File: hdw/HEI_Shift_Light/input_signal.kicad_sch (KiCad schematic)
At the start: 20 parts

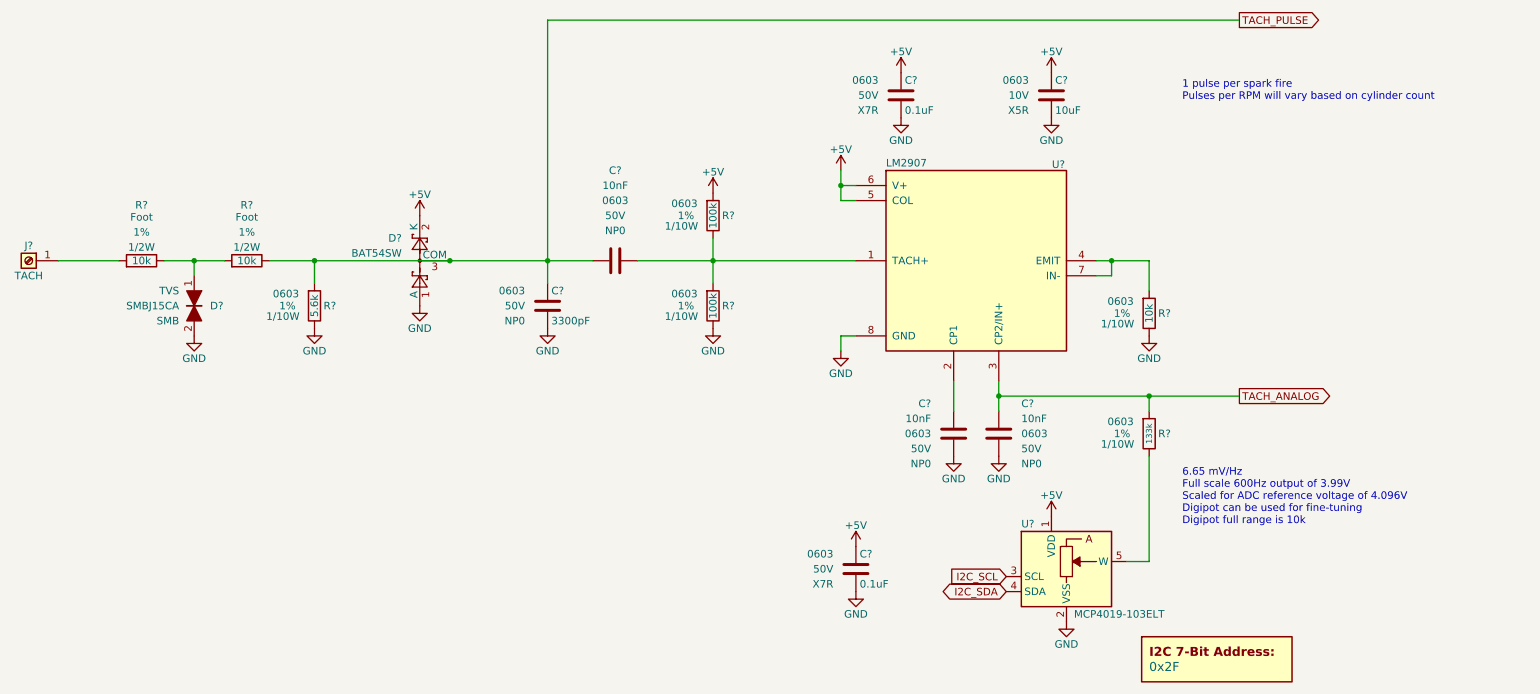
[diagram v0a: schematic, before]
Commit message: filled in digikey part numbers
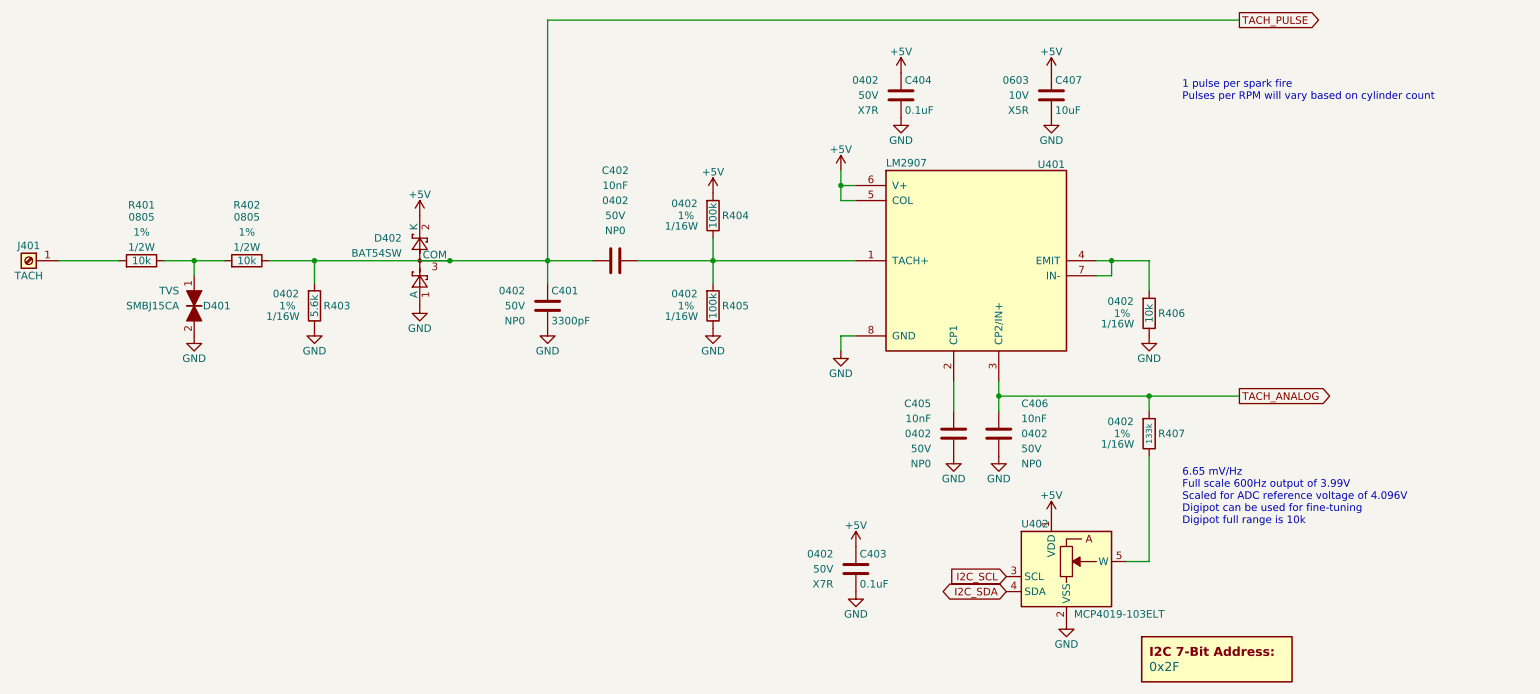
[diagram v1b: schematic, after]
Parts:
- C401: renamed from C?; footprint (none) -> Capacitors_SMD:C_0402; Digi-Key PN PN -> 311-3968-1-ND; display_footprint 0603 -> 0402
- C402, C405, C406: renamed from C?; footprint (none) -> Capacitors_SMD:C_0402; display_footprint 0603 -> 0402
- C403, C404: renamed from C?; footprint Capacitors_SMD:C_0603 -> Capacitors_SMD:C_0402; display_footprint 0603 -> 0402
- D401: renamed from D?; Digi-Key PN (none) -> SMBJ15CA-E3-52GICT-ND; Footprint Display SMB -> (none); display_footprint (none) -> SMB
- D402: renamed from D?; Digi-Key PN (none) -> 568-1615-1-ND
- J401: renamed from J?; footprint (none) -> Keystone:7691; Digi-Key PN (none) -> 36-7691-ND; MPN (none) -> 7691; Manufacturer (none) -> Keystone Electronics
- R401, R402: renamed from R?; footprint (none) -> Resistors_SMD:R_0805; Digi-Key PN (none) -> 541-10.0KLCT-ND; display_footprint Foot -> 0805
- R403: renamed from R?; footprint Resistors_SMD:R_0603 -> Resistors_SMD:R_0402; Digi-Key PN (none) -> 541-5.60KLCT-ND; Wattage 1/10W -> 1/16W; display_footprint 0603 -> 0402
- R404, R405: renamed from R?; footprint Resistors_SMD:R_0603 -> Resistors_SMD:R_0402; Digi-Key PN (none) -> 541-100KLCT-ND; Wattage 1/10W -> 1/16W; display_footprint 0603 -> 0402
- R406: renamed from R?; footprint Resistors_SMD:R_0603 -> Resistors_SMD:R_0402; Digi-Key PN 541-10.0KHCT-ND -> 541-10.0KLCT-ND; Wattage 1/10W -> 1/16W; display_footprint 0603 -> 0402
- R407: renamed from R?; footprint Resistors_SMD:R_0603 -> Resistors_SMD:R_0402; Digi-Key PN (none) -> 541-133KLCT-ND; Wattage 1/10W -> 1/16W; display_footprint 0603 -> 0402
- U401: renamed from U?; Digi-Key PN (none) -> LM2907N-8-NOPB-ND
- gave numbers to parts that had none: 3

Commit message: fixed a few digikey pns
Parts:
- R401, R402: Digi-Key PN 541-10.0KLCT-ND -> P16059CT-ND; MPN (none) -> CRCW080510K0FKEA
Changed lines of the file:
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@@
 			)
 		)
-		(property "Digi-Key PN" "541-10.0KLCT-ND"
+		(property "Digi-Key PN" "P16059CT-ND"
 			(at 30.48 101.6 0)
 			(hide yes)
@@
 			)
 		)
+    (property "MPN" "CRCW080510K0FKEA" (at 40.64 93.98 0)
+      (effects (font (size 1.27 1.27)) (hide yes))
+    )
 		(pin "1"
 		)
@@
 			)
 		)
-		(property "Digi-Key PN" "541-10.0KLCT-ND"
+		(property "Digi-Key PN" "P16059CT-ND"
 			(at 48.26 101.6 0)
 			(hide yes)
@@
 			)
 		)
-		(pin "1"
-		)
+    (property "MPN" "CRCW080510K0FKEA" (at 58.42 93.98 0)
+      (effects (font (size 1.27 1.27)) (hide yes))
+    )
+		(pin "1"
+		)

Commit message: Added input signal path simulation
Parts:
- C406: value 10nF -> 1uF; Digi-Key PN 311-3960-1-ND -> (none); display_footprint 0402 -> (none)
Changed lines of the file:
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@@
 			)
 		)
-    (property "Digi-Key PN" "SMBJ15CA-E3-52GICT-ND" (at 49.53 101.6 0)
-      (effects (font (size 1.27 1.27)) (hide yes))
-    )
+		(property "Digi-Key PN" "SMBJ15CA-E3-52GICT-ND"
+			(at 49.53 101.6 0)
+			(hide yes)
+			(show_name no)
+			(do_not_autoplace no)
+			(effects
+				(font
+					(size 1.27 1.27)
+				)
+			)
+		)
 		(pin "1"
 		)
@@
 			)
 		)
-    (property "MPN" "CRCW080510K0FKEA" (at 40.64 93.98 0)
-      (effects (font (size 1.27 1.27)) (hide yes))
-    )
+		(property "MPN" "CRCW080510K0FKEA"
+			(at 40.64 93.98 0)
+			(hide yes)
+			(show_name no)
+			(do_not_autoplace no)
+			(effects
+				(font
+					(size 1.27 1.27)
+				)
+			)
+		)
 		(pin "1"
 		)
@@
 			)
 		)
-    (property "Digi-Key PN" "568-1615-1-ND" (at 87.63 93.98 0)
-      (effects (font (size 1.27 1.27)) (hide yes))
-    )
+		(property "Digi-Key PN" "568-1615-1-ND"
+			(at 87.63 93.98 0)
+			(hide yes)
+			(show_name no)
+			(do_not_autoplace no)
+			(effects
+				(font
+					(size 1.27 1.27)
+				)
+			)
+		)
 		(pin "1"
 		)
@@
 			)
 		)
-    (property "Digi-Key PN" "LM2907N-8-NOPB-ND" (at 181.61 93.98 0)
-      (effects (font (size 1.27 1.27)) (hide yes))
-    )
+		(property "Digi-Key PN" "LM2907N-8-NOPB-ND"
+			(at 181.61 93.98 0)
+			(hide yes)
+			(show_name no)
+			(do_not_autoplace no)
+			(effects
+				(font
+					(size 1.27 1.27)
+				)
+			)
+		)
 		(pin "7"
 		)
@@
 			)
 		)
-		(property "Value" "10nF"
+		(property "Value" "1uF"
 			(at 189.23 120.6499 0)
 			(show_name no)
@@
 			)
 		)
-		(property "display_footprint" "0402"
+		(property "display_footprint" ""
 			(at 189.23 123.1899 0)
 			(show_name no)
@@
 			)
 		)
-		(property "Digi-Key PN" "311-3960-1-ND"
+		(property "Digi-Key PN" ""
 			(at 196.215 110.49 0)
 			(hide yes)
@@
 			)
 		)
-    (property "Digi-Key PN" "36-7691-ND" (at 21.59 93.98 0)
-      (effects (font (size 1.27 1.27)) (hide yes))
-    )
-    (property "MPN" "7691" (at 21.59 93.98 0)
-      (effects (font (size 1.27 1.27)) (hide yes))
-    )
-    (property "Manufacturer" "Keystone Electronics" (at 21.59 93.98 0)
-      (effects (font (size 1.27 1.27)) (hide yes))
-    )
+		(property "Digi-Key PN" "36-7691-ND"
+			(at 21.59 93.98 0)
+			(hide yes)
+			(show_name no)
+			(do_not_autoplace no)
+			(effects
+				(font
+					(size 1.27 1.27)
+				)
+			)
+		)
+		(property "MPN" "7691"
+			(at 21.59 93.98 0)
+			(hide yes)
+			(show_name no)
+			(do_not_autoplace no)
+			(effects
+				(font
+					(size 1.27 1.27)
+				)
+			)
+		)
+		(property "Manufacturer" "Keystone Electronics"
+			(at 21.59 93.98 0)
+			(hide yes)
+			(show_name no)
+			(do_not_autoplace no)
+			(effects
+				(font
+					(size 1.27 1.27)
+				)
+			)
+		)
 		(pin "1"
 		)
@@
 			)
 		)
-    (property "MPN" "CRCW080510K0FKEA" (at 58.42 93.98 0)
-      (effects (font (size 1.27 1.27)) (hide yes))
-    )
+		(property "MPN" "CRCW080510K0FKEA"
+			(at 58.42 93.98 0)
+			(hide yes)
+			(show_name no)
+			(do_not_autoplace no)
+			(effects
+				(font
+					(size 1.27 1.27)
+				)
+			)
+		)
 		(pin "1"
 		)

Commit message: change LM2907 filter cap to 10uF
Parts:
- removed C406: 1uF, Capacitors_SMD:C_0402, symbol Custom Library:C_Custom
- added C406: 10uF, Capacitors_SMD:C_0603, symbol Custom_Library:C_Custom
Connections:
- net GND: now also C406.2
- net TACH_ANALOG: now also C406.1
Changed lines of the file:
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@@
-	)
-	(symbol
-		(lib_id "Custom Library:C_Custom")
-		(at 185.42 123.19 0)
-		(unit 1)
-		(body_style 1)
-		(exclude_from_sim no)
-		(in_bom yes)
-		(on_board yes)
-		(in_pos_files yes)
-		(dnp no)
-		(property "Reference" "C406"
-			(at 189.23 118.1099 0)
-			(show_name no)
-			(do_not_autoplace no)
-			(effects
-				(font
-					(size 1.27 1.27)
-				)
-				(justify left)
-			)
-		)
-		(property "Value" "1uF"
-			(at 189.23 120.6499 0)
-			(show_name no)
-			(do_not_autoplace no)
-			(effects
-				(font
-					(size 1.27 1.27)
-				)
-				(justify left)
-			)
-		)
-		(property "Footprint" "Capacitors_SMD:C_0402"
-			(at 186.3852 127 0)
-			(hide yes)
-			(show_name no)
-			(do_not_autoplace no)
-			(effects
-				(font
-					(size 1.27 1.27)
-				)
-			)
-		)
-		(property "Datasheet" ""
-			(at 186.055 120.65 0)
-			(hide yes)
-			(show_name no)
-			(do_not_autoplace no)
-			(effects
-				(font
-					(size 1.27 1.27)
-				)
-			)
-		)
-		(property "Description" "Unpolarized capacitor"
-			(at 185.42 123.19 0)
-			(hide yes)
-			(show_name no)
-			(do_not_autoplace no)
-			(effects
-				(font
-					(size 1.27 1.27)
-				)
-			)
-		)
-		(property "display_footprint" ""
-			(at 189.23 123.1899 0)
-			(show_name no)
-			(do_not_autoplace no)
-			(effects
-				(font
-					(size 1.27 1.27)
-				)
-				(justify left)
-			)
-		)
-		(property "Voltage" "50V"
-			(at 189.23 125.7299 0)
-			(show_name no)
-			(do_not_autoplace no)
-			(effects
-				(font
-					(size 1.27 1.27)
-				)
-				(justify left)
-			)
-		)
-		(property "Dielectric" "NP0"
-			(at 189.23 128.2699 0)
-			(show_name no)
-			(do_not_autoplace no)
-			(effects
-				(font
-					(size 1.27 1.27)
-				)
-				(justify left)
-			)
-		)
-		(property "Digi-Key PN" ""
-			(at 196.215 110.49 0)
-			(hide yes)
-			(show_name no)
-			(do_not_autoplace no)
-			(effects
-				(font
-					(size 1.524 1.524)
-				)
-			)
-		)
-		(pin "1"
-		)
-		(pin "2"
-		)
-		(instances
-			(project "HEI_Shift_Light"
-				(path "/288c8230-69eb-4ad9-929d-f4630114196f/3f3e3aac-043b-4713-af21-26e9e85000ef"
-					(reference "C406")
-					(unit 1)
-				)
-			)
-		)
 	)
 	(symbol
@@
 					(unit 1)
 				)
+			)
+		)
+	)
+	(symbol
+		(lib_id "Custom_Library:C_Custom")
+		(at 185.42 123.19 0)
+		(unit 1)
+		(body_style 1)
+		(exclude_from_sim no)
+		(in_bom yes)
+		(on_board yes)
+		(in_pos_files yes)
+		(dnp no)
+		(fields_autoplaced yes)
+		(property "Reference" "C406"
+			(at 189.23 118.1099 0)
+			(show_name no)
+			(do_not_autoplace no)
+			(effects
+				(font
+					(size 1.27 1.27)
+				)
+				(justify left)
+			)
+		)
+		(property "Value" "10uF"
+			(at 189.23 120.6499 0)
+			(show_name no)
+			(do_not_autoplace no)
+			(effects
+				(font
+					(size 1.27 1.27)
+				)
+				(justify left)
+			)
+		)
+		(property "Footprint" "Capacitors_SMD:C_0603"
+			(at 186.3852 127 0)
+			(hide yes)
+			(show_name no)
+			(do_not_autoplace no)
+			(effects
+				(font
+					(size 1.27 1.27)
+				)
+			)
+		)
+		(property "Datasheet" ""
+			(at 186.055 120.65 0)
+			(hide yes)
+			(show_name no)
+			(do_not_autoplace no)
+			(effects
+				(font
+					(size 1.27 1.27)
+				)
+			)
+		)
+		(property "Description" ""
+			(at 185.42 123.19 0)
+			(show_name no)
+			(do_not_autoplace no)
+			(effects
+				(font
+					(size 1.27 1.27)
+				)
+			)
+		)
+		(property "display_footprint" "0603"
+			(at 189.23 123.1899 0)
+			(show_name no)
+			(do_not_autoplace no)
+			(effects
+				(font
+					(size 1.27 1.27)
+				)
+				(justify left)
+			)
+		)
+		(property "Voltage" "10V"
+			(at 189.23 125.7299 0)
+			(show_name no)
+			(do_not_autoplace no)
+			(effects
+				(font
+					(size 1.27 1.27)
+				)
+				(justify left)
+			)
+		)
+		(property "Dielectric" "X5R"
+			(at 189.23 128.2699 0)
+			(show_name no)
+			(do_not_autoplace no)
+			(effects
+				(font
+					(size 1.27 1.27)
+				)
+				(justify left)
+			)
+		)
+		(property "Digi-Key PN" "490-10474-1-ND"
+			(at 185.42 123.19 0)
+			(hide yes)
+			(show_name no)
+			(do_not_autoplace no)
+			(effects
+				(font
+					(size 1.27 1.27)
+				)
+			)
+		)
+		(pin "1"
+		)
+		(pin "2"
+		)
+		(instances
+			(project "HEI_Shift_Light"
+				(path "/288c8230-69eb-4ad9-929d-f4630114196f/3f3e3aac-043b-4713-af21-26e9e85000ef"
+					(reference "C406")
+					(unit 1)
+				)

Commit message: fixed some digikey pns
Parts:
- C401: Digi-Key PN 311-3968-1-ND -> 490-GRM1555C1H332GE01DTR-ND
- C403, C404: Digi-Key PN 399-7845-1-ND -> 1276-7069-1-ND
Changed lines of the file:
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@@
 			)
 		)
-		(property "Digi-Key PN" "399-7845-1-ND"
+		(property "Digi-Key PN" "1276-7069-1-ND"
 			(at 179.705 53.34 0)
 			(hide yes)
@@
 			)
 		)
-		(property "Digi-Key PN" "311-3968-1-ND"
+		(property "Digi-Key PN" "490-GRM1555C1H332GE01DTR-ND"
 			(at 120.015 88.9 0)
 			(hide yes)
@@
 			)
 		)
-		(property "Digi-Key PN" "399-7845-1-ND"
+		(property "Digi-Key PN" "1276-7069-1-ND"
 			(at 172.085 133.35 0)
 			(hide yes)

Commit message: added component datasheet properties
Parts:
- C403, C404: Digi-Key PN 1276-7069-1-ND -> 445-5932-1-ND
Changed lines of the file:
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@@
 			)
 		)
-		(property "Datasheet" ""
+		(property "Datasheet" "https://www.vishay.com/docs/88392/smbj.pdf"
 			(at 53.34 101.6 0)
 			(show_name no)
@@
 			)
 		)
-		(property "Datasheet" ""
+		(property "Datasheet" "https://product.tdk.com/en/system/files/dam/doc/product/capacitor/ceramic/mlcc/charasheet/c1005x7r1h104k050bb.pdf"
 			(at 169.545 63.5 0)
 			(hide yes)
@@
 			)
 		)
-		(property "Digi-Key PN" "1276-7069-1-ND"
+		(property "Digi-Key PN" "445-5932-1-ND"
 			(at 179.705 53.34 0)
 			(hide yes)
@@
 			)
 		)
-		(property "Datasheet" ""
+		(property "Datasheet" "https://www.vishay.com/docs/20035/dcrcwe3.pdf"
 			(at 210.82 123.19 0)
 			(hide yes)
@@
 			)
 		)
-		(property "Datasheet" ""
+		(property "Datasheet" "https://industrial.panasonic.com/cdbs/www-data/pdf/AQA0000/AQA0000CE21.pdf"
 			(at 40.64 93.98 0)
 			(hide yes)
@@
 			)
 		)
-		(property "Datasheet" ""
+		(property "Datasheet" "https://www.vishay.com/docs/20035/dcrcwe3.pdf"
 			(at 137.16 101.6 0)
 			(hide yes)
@@
 			)
 		)
-		(property "Datasheet" ""
+		(property "Datasheet" "https://www.vishay.com/docs/20035/dcrcwe3.pdf"
 			(at 137.16 86.36 0)
 			(hide yes)
@@
 			)
 		)
-		(property "Datasheet" ""
+		(property "Datasheet" "https://search.murata.co.jp/Ceramy/image/img/A01X/G101/ENG/GRM1555C1H332GE01-01A.pdf"
 			(at 109.855 99.06 0)
 			(hide yes)
@@
 			)
 		)
-		(property "Datasheet" ""
+		(property "Datasheet" "https://product.tdk.com/en/system/files/dam/doc/product/capacitor/ceramic/mlcc/charasheet/c1005x7r1h104k050bb.pdf"
 			(at 161.925 143.51 0)
 			(hide yes)
@@
 			)
 		)
-		(property "Digi-Key PN" "1276-7069-1-ND"
+		(property "Digi-Key PN" "445-5932-1-ND"
 			(at 172.085 133.35 0)
 			(hide yes)
@@
 			)
 		)
-		(property "Datasheet" ""
+		(property "Datasheet" "https://search.murata.co.jp/Ceramy/image/img/A01X/G101/ENG/GRM188R61A106KE69-01.pdf"
 			(at 194.945 63.5 0)
 			(hide yes)
@@
 			)
 		)
-		(property "Datasheet" ""
+		(property "Datasheet" "https://search.murata.co.jp/Ceramy/image/img/A01X/G101/ENG/GRM188R61A106KE69-01.pdf"
 			(at 186.055 120.65 0)
 			(hide yes)
@@
 			)
 		)
-		(property "Datasheet" ""
+		(property "Datasheet" "https://www.yageo.com/en/Chart/Download/pdf/CC0603JRNPO9BN103"
 			(at 118.11 94.615 0)
 			(hide yes)
@@
 			)
 		)
-		(property "Datasheet" ""
+		(property "Datasheet" "https://www.vishay.com/docs/20035/dcrcwe3.pdf"
 			(at 69.85 101.6 0)
 			(hide yes)
@@
 			)
 		)
-		(property "Datasheet" ""
+		(property "Datasheet" "https://www.vishay.com/docs/20035/dcrcwe3.pdf"
 			(at 210.82 102.87 0)
 			(hide yes)
@@
 			)
 		)
-		(property "Datasheet" ""
+		(property "Datasheet" "https://www.yageo.com/en/Chart/Download/pdf/CC0603JRNPO9BN103"
 			(at 177.165 120.65 0)
 			(hide yes)
@@
 			)
 		)
-		(property "Datasheet" ""
+		(property "Datasheet" "https://www.keyelco.com/userAssets/file/K75p73.pdf"
 			(at 21.59 93.98 0)
 			(hide yes)
@@
 			)
 		)
-		(property "Datasheet" ""
+		(property "Datasheet" "https://industrial.panasonic.com/cdbs/www-data/pdf/AQA0000/AQA0000CE21.pdf"
 			(at 58.42 93.98 0)
 			(hide yes)

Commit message: updated a lot of font, table of contents
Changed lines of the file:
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@@
 	(title_block
 		(title "HEI Shift Light")
-		(date "2026-05-29")
+		(date "2026-06-02")
 		(rev "A")
 		(company "Drew Maatman")
@@
 		(effects
 			(font
+				(face "Arial")
 				(size 1.27 1.27)
 			)
@@
 		(effects
 			(font
+				(face "Arial")
 				(size 1.27 1.27)
 			)
@@
 		(property "Datasheet" "https://www.vishay.com/docs/88392/smbj.pdf"
 			(at 53.34 101.6 0)
-			(show_name no)
-			(do_not_autoplace no)
+			(hide yes)
+			(show_name no)
+			(do_not_autoplace no)

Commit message: cleaned up digikey pns
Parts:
- C402, C405: Digi-Key PN 311-3960-1-ND -> 1276-1028-1-ND
- C406, C407: Digi-Key PN 490-10474-1-ND -> 445-C1608X5R1A106K080ACCT-ND
- D401: Digi-Key PN SMBJ15CA-E3-52GICT-ND -> SMBJ15CA
- D402: Digi-Key PN 568-1615-1-ND -> BAT54SWT1GOSCT-ND
- U401: Digi-Key PN LM2907N-8-NOPB-ND -> LM2907MX-8/NOPBCT-ND
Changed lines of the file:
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@@
 		(property "Intersheetrefs" "${INTERSHEET_REFS}"
 			(at 174.9735 149.86 0)
-			(hide yes)
 			(show_name no)
 			(do_not_autoplace no)
@@
 		(property "Intersheetrefs" "${INTERSHEET_REFS}"
 			(at 241.8058 116.84 0)
-			(hide yes)
 			(show_name no)
 			(do_not_autoplace no)
@@
 		(property "Intersheetrefs" "${INTERSHEET_REFS}"
 			(at 176.1453 147.32 0)
-			(hide yes)
 			(show_name no)
 			(do_not_autoplace no)
@@
 		(property "Intersheetrefs" "${INTERSHEET_REFS}"
 			(at 240.6566 53.34 0)
-			(hide yes)
 			(show_name no)
 			(do_not_autoplace no)
@@
 			)
 		)
-		(property "Digi-Key PN" "SMBJ15CA-E3-52GICT-ND"
+		(property "Digi-Key PN" "SMBJ15CA"
 			(at 49.53 101.6 0)
 			(hide yes)
@@
 			)
 		)
-		(property "Digi-Key PN" "568-1615-1-ND"
+		(property "Digi-Key PN" "BAT54SWT1GOSCT-ND"
 			(at 87.63 93.98 0)
 			(hide yes)
@@
 			)
 		)
-		(property "Digi-Key PN" "LM2907N-8-NOPB-ND"
+		(property "Digi-Key PN" "LM2907MX-8/NOPBCT-ND"
 			(at 181.61 93.98 0)
 			(hide yes)
@@
 			)
 		)
-		(property "Digi-Key PN" "490-10474-1-ND"
+		(property "Digi-Key PN" "445-C1608X5R1A106K080ACCT-ND"
 			(at 194.31 66.04 0)
 			(hide yes)
@@
 			)
 		)
-		(property "Digi-Key PN" "490-10474-1-ND"
+		(property "Digi-Key PN" "445-C1608X5R1A106K080ACCT-ND"
 			(at 185.42 123.19 0)
 			(hide yes)
@@
 			)
 		)
-		(property "Digi-Key PN" "311-3960-1-ND"
+		(property "Digi-Key PN" "1276-1028-1-ND"
 			(at 107.95 104.775 0)
 			(hide yes)
@@
 			)
 		)
-		(property "Digi-Key PN" "311-3960-1-ND"
+		(property "Digi-Key PN" "1276-1028-1-ND"
 			(at 167.005 110.49 0)
 			(hide yes)
